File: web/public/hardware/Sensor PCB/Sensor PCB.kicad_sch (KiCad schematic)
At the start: 20 parts, among them J1 Conn_01x08_Pin, J2 Conn_01x08_Pin, J3 Conn_01x06_Pin, J4 Conn_01x06_Pin, U1 DRV5033AJxDBZ, U2 DRV5033AJxDBZ, U3 DRV5033AJxDBZ, U4 DRV5033AJxDBZ, U5 74LS11, U6 74LS11

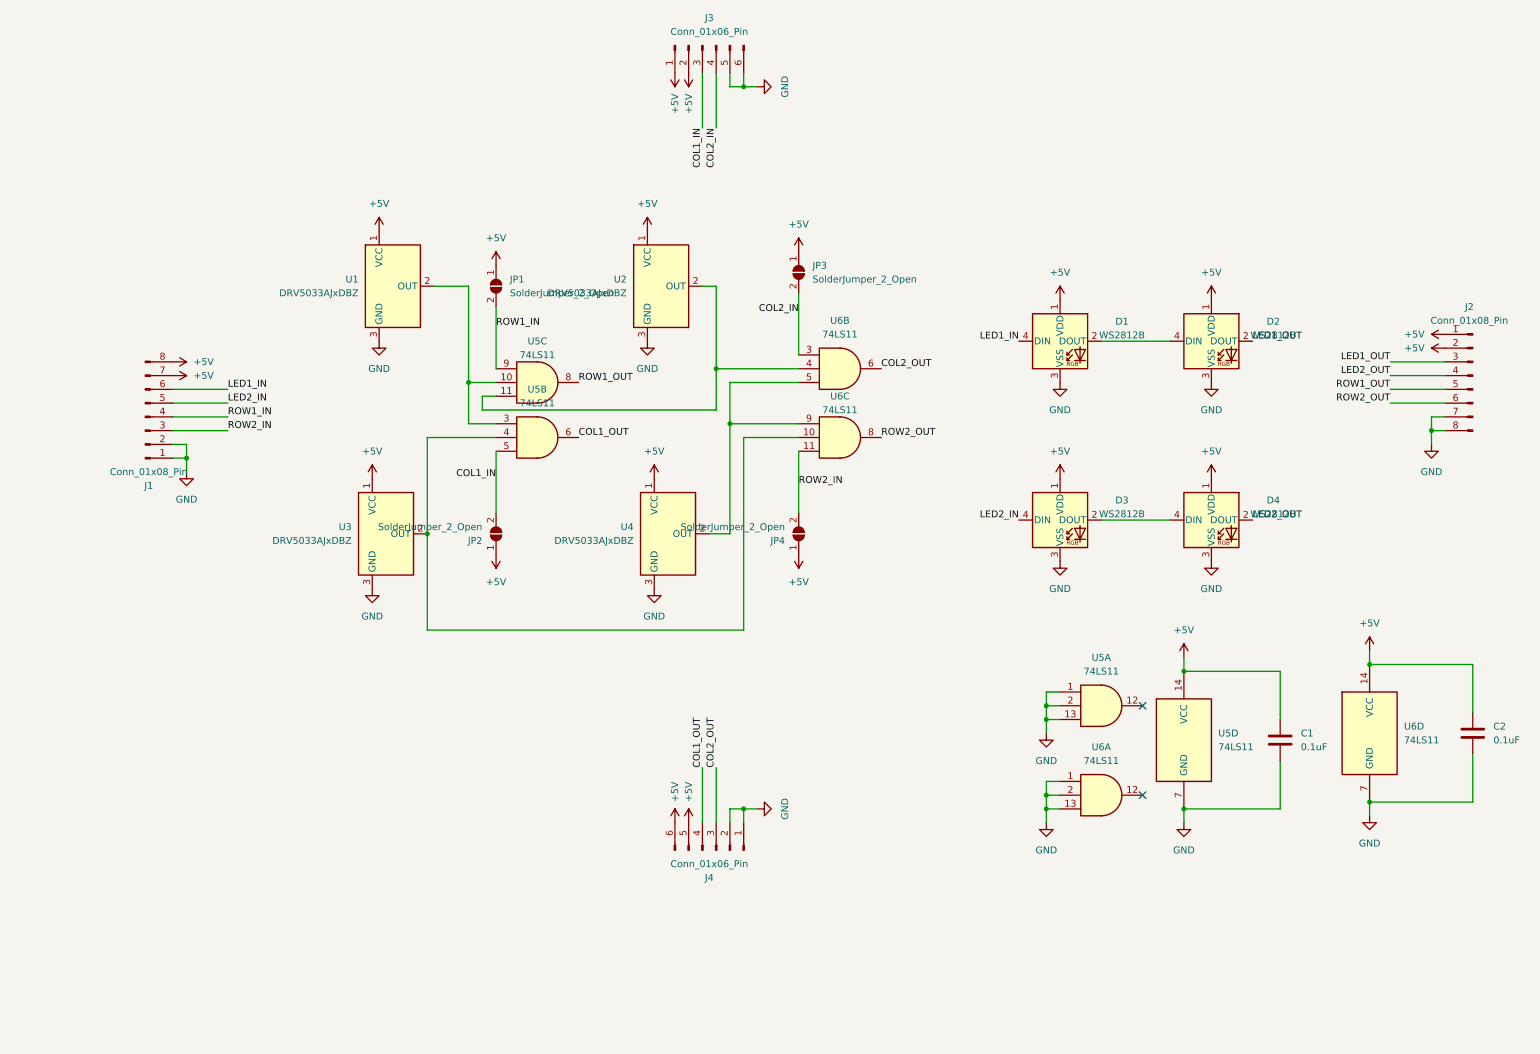
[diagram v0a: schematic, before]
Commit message: Route PCB power and change sch/PCB page size to US letter
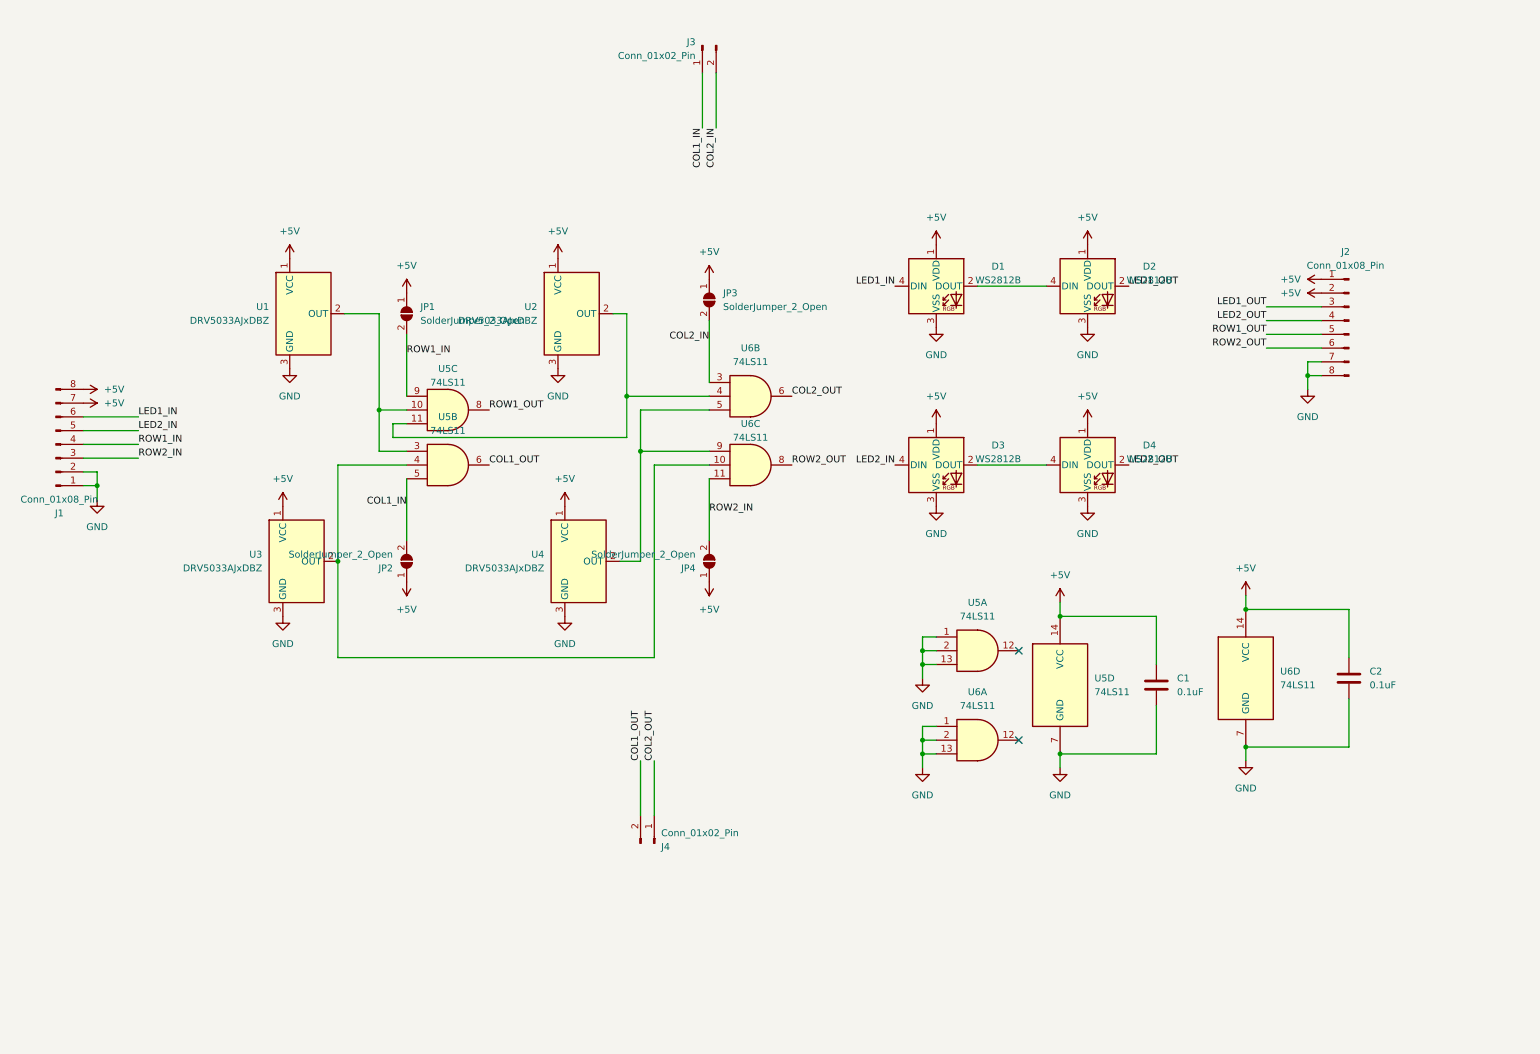
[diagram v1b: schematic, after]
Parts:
- removed J3, J4: Conn_01x06_Pin, Connector_PinHeader_2.54mm:PinHeader_1x06_P2.54mm_Horizontal, symbol Connector:Conn_01x06_Pin
- added J3, J4: Conn_01x02_Pin, Connector_PinHeader_2.54mm:PinHeader_1x02_P2.54mm_Horizontal, symbol Connector:Conn_01x02_Pin
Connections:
- net COL1_IN: now also J3.1 (Pin_1)
- net COL1_OUT: now also J4.2 (Pin_2)
- net COL2_IN: now also J3.2 (Pin_2)
- net COL2_OUT: now also J4.1 (Pin_1)
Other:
- company: (none) -> ECE 477
- title: (none) -> Sensor PCB
- moved on the sheet: C1, C2, D1, D2, D3, D4, J1, J2, JP1, JP2, JP3, JP4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

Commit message: Update production files
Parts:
- added H1, H2, H3: MountingHole, MountingHole:MountingHole_2.7mm_M2.5, symbol Mechanical:MountingHole
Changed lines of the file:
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@@
+    )
+  )
+  (symbol (lib_id "Mechanical:MountingHole") (at 38.1 185.42 0) (unit 1)
+    (in_bom yes) (on_board yes) (dnp no) (fields_autoplaced)
+    (property "Reference" "H3" (at 40.64 184.15 0)
+      (effects (font (size 1.27 1.27)) (justify left))
+    )
+    (property "Value" "MountingHole" (at 40.64 186.69 0)
+      (effects (font (size 1.27 1.27)) (justify left))
+    )
+    (property "Footprint" "MountingHole:MountingHole_2.7mm_M2.5" (at 38.1 185.42 0)
+      (effects (font (size 1.27 1.27)) hide)
+    )
+    (property "Datasheet" "~" (at 38.1 185.42 0)
+      (effects (font (size 1.27 1.27)) hide)
+    )
+    (instances
+      (project "Sensor PCB"
+        (path "/a9f063f9-73a8-44d6-aee6-f41a657d12c2"
+          (reference "H3") (unit 1)
+        )
+      )
     )
   )
@@
     )
   )
+  (symbol (lib_id "Mechanical:MountingHole") (at 38.1 179.07 0) (unit 1)
+    (in_bom yes) (on_board yes) (dnp no) (fields_autoplaced)
+    (property "Reference" "H2" (at 40.64 177.8 0)
+      (effects (font (size 1.27 1.27)) (justify left))
+    )
+    (property "Value" "MountingHole" (at 40.64 180.34 0)
+      (effects (font (size 1.27 1.27)) (justify left))
+    )
+    (property "Footprint" "MountingHole:MountingHole_2.7mm_M2.5" (at 38.1 179.07 0)
+      (effects (font (size 1.27 1.27)) hide)
+    )
+    (property "Datasheet" "~" (at 38.1 179.07 0)
+      (effects (font (size 1.27 1.27)) hide)
+    )
+    (instances
+      (project "Sensor PCB"
+        (path "/a9f063f9-73a8-44d6-aee6-f41a657d12c2"
+          (reference "H2") (unit 1)
+        )
+      )
+    )
+  )
   (symbol (lib_id "power:GND") (at 59.69 121.92 0) (unit 1)
     (in_bom yes) (on_board yes) (dnp no) (fields_autoplaced)
@@
         )
       )
+    )
+  )
+  (symbol (lib_id "Mechanical:MountingHole") (at 38.1 172.72 0) (unit 1)
+    (in_bom yes) (on_board yes) (dnp no) (fields_autoplaced)
+    (property "Reference" "H1" (at 40.64 171.45 0)
+      (effects (font (size 1.27 1.27)) (justify left))
+    )
+    (property "Value" "MountingHole" (at 40.64 173.99 0)
+      (effects (font (size 1.27 1.27)) (justify left))
+    )
+    (property "Footprint" "MountingHole:MountingHole_2.7mm_M2.5" (at 38.1 172.72 0)
+      (effects (font (size 1.27 1.27)) hide)
+    )
+    (property "Datasheet" "~" (at 38.1 172.72 0)
+      (effects (font (size 1.27 1.27)) hide)
+    )
+    (instances
+      (project "Sensor PCB"
+        (path "/a9f063f9-73a8-44d6-aee6-f41a657d12c2"
+          (reference "H1") (unit 1)
+        )
+      )

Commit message: Add pullup resistor to hall effect sensor for open-drain sensors
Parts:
- added R1, R2, R3, R4: 10K, Resistor_SMD:R_0805_2012Metric_Pad1.20x1.40mm_HandSolder, symbol Device:R_Small_US
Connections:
- net +5V: now also R1.1, R2.1, R3.1, R4.1
- net at U2.2 (OUT), U5.11, U6.4: now also R2.2
- net at U4.2 (OUT), U6.5, U6.9: now also R4.2
- net at U1.2 (OUT), U5.10, U5.3: now also R1.2
- net at U3.2 (OUT), U5.4, U6.10: now also R3.2
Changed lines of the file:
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@@
   (junction (at 177.8 144.78) (diameter 0) (color 0 0 0 0)
   )
+  (junction (at 123.19 111.76) (diameter 0) (color 0 0 0 0)
+  )
   (junction (at 237.49 146.05) (diameter 0) (color 0 0 0 0)
   )
@@
   (junction (at 77.47 83.82) (diameter 0) (color 0 0 0 0)
   )
+  (junction (at 69.85 93.98) (diameter 0) (color 0 0 0 0)
+  )
   (junction (at 25.4 97.79) (diameter 0) (color 0 0 0 0)
   )
+  (junction (at 123.19 66.04) (diameter 0) (color 0 0 0 0)
+  )
   (junction (at 203.2 147.32) (diameter 0) (color 0 0 0 0)
   )
   (junction (at 177.8 130.81) (diameter 0) (color 0 0 0 0)
+  )
+  (junction (at 73.66 66.04) (diameter 0) (color 0 0 0 0)
   )
   (junction (at 248.92 77.47) (diameter 0) (color 0 0 0 0)
@@
     (stroke (width 0) (type default))
   )
-  (wire (pts (xy 121.92 111.76) (xy 125.73 111.76))
+  (wire (pts (xy 123.19 55.88) (xy 123.19 58.42))
+    (stroke (width 0) (type default))
+  )
+  (wire (pts (xy 121.92 111.76) (xy 123.19 111.76))
     (stroke (width 0) (type default))
   )
@@
     (stroke (width 0) (type default))
   )
+  (wire (pts (xy 69.85 91.44) (xy 69.85 93.98))
+    (stroke (width 0) (type default))
+  )
   (wire (pts (xy 80.01 88.9) (xy 123.19 88.9))
     (stroke (width 0) (type default))
   )
+  (wire (pts (xy 123.19 109.22) (xy 123.19 111.76))
+    (stroke (width 0) (type default))
+  )
   (wire (pts (xy 177.8 147.32) (xy 180.34 147.32))
     (stroke (width 0) (type default))
@@
     (stroke (width 0) (type default))
   )
-  (wire (pts (xy 71.12 66.04) (xy 77.47 66.04))
+  (wire (pts (xy 73.66 63.5) (xy 73.66 66.04))
+    (stroke (width 0) (type default))
+  )
+  (wire (pts (xy 71.12 66.04) (xy 73.66 66.04))
     (stroke (width 0) (type default))
   )
@@
     (stroke (width 0) (type default))
   )
+  (wire (pts (xy 123.19 111.76) (xy 125.73 111.76))
+    (stroke (width 0) (type default))
+  )
   (wire (pts (xy 251.46 77.47) (xy 248.92 77.47))
     (stroke (width 0) (type default))
@@
     (stroke (width 0) (type default))
   )
+  (wire (pts (xy 123.19 101.6) (xy 123.19 104.14))
+    (stroke (width 0) (type default))
+  )
   (wire (pts (xy 125.73 91.44) (xy 138.43 91.44))
     (stroke (width 0) (type default))
@@
     (stroke (width 0) (type default))
   )
+  (wire (pts (xy 73.66 66.04) (xy 77.47 66.04))
+    (stroke (width 0) (type default))
+  )
+  (wire (pts (xy 69.85 83.82) (xy 69.85 86.36))
+    (stroke (width 0) (type default))
+  )
   (wire (pts (xy 25.4 95.25) (xy 25.4 97.79))
     (stroke (width 0) (type default))
@@
   )
   (wire (pts (xy 248.92 77.47) (xy 248.92 80.01))
+    (stroke (width 0) (type default))
+  )
+  (wire (pts (xy 123.19 63.5) (xy 123.19 66.04))
+    (stroke (width 0) (type default))
+  )
+  (wire (pts (xy 73.66 55.88) (xy 73.66 58.42))
     (stroke (width 0) (type default))
   )
@@
   (label "COL2_OUT" (at 153.67 81.28 0) (fields_autoplaced)
     (effects (font (size 1.27 1.27)) (justify left bottom))
+  )
+  (symbol (lib_id "power:+5V") (at 73.66 55.88 0) (unit 1)
+    (in_bom yes) (on_board yes) (dnp no)
+    (property "Reference" "#PWR025" (at 73.66 59.69 0)
+      (effects (font (size 1.27 1.27)) hide)
+    )
+    (property "Value" "+5V" (at 73.66 52.07 0)
+      (effects (font (size 1.27 1.27)))
+    )
+    (property "Footprint" "" (at 73.66 55.88 0)
+      (effects (font (size 1.27 1.27)) hide)
+    )
+    (property "Datasheet" "" (at 73.66 55.88 0)
+      (effects (font (size 1.27 1.27)) hide)
+    )
+    (pin "1")
+    (instances
+      (project "Sensor PCB"
+        (path "/a9f063f9-73a8-44d6-aee6-f41a657d12c2"
+          (reference "#PWR025") (unit 1)
+        )
+      )
+    )
   )
   (symbol (lib_id "power:+5V") (at 251.46 62.23 90) (mirror x) (unit 1)
@@
     )
   )
+  (symbol (lib_id "Device:R_Small_US") (at 123.19 106.68 0) (unit 1)
+    (in_bom yes) (on_board yes) (dnp no) (fields_autoplaced)
+    (property "Reference" "R4" (at 125.73 105.41 0)
+      (effects (font (size 1.27 1.27)) (justify left))
+    )
+    (property "Value" "10K" (at 125.73 107.95 0)
+      (effects (font (size 1.27 1.27)) (justify left))
+    )
+    (property "Footprint" "Resistor_SMD:R_0805_2012Metric_Pad1.20x1.40mm_HandSolder" (at 123.19 106.68 0)
+      (effects (font (size 1.27 1.27)) hide)
+    )
+    (property "Datasheet" "~" (at 123.19 106.68 0)
+      (effects (font (size 1.27 1.27)) hide)
+    )
+    (pin "1")
+    (pin "2")
+    (instances
+      (project "Sensor PCB"
+        (path "/a9f063f9-73a8-44d6-aee6-f41a657d12c2"
+          (reference "R4") (unit 1)
+        )
+      )
+    )
+  )
   (symbol (lib_id "power:GND") (at 180.34 68.58 0) (mirror y) (unit 1)
     (in_bom yes) (on_board yes) (dnp no) (fields_autoplaced)
@@
         (path "/a9f063f9-73a8-44d6-aee6-f41a657d12c2"
           (reference "#PWR021") (unit 1)
+        )
+      )
+    )
+  )
+  (symbol (lib_id "power:+5V") (at 123.19 101.6 0) (unit 1)
+    (in_bom yes) (on_board yes) (dnp no)
+    (property "Reference" "#PWR028" (at 123.19 105.41 0)
+      (effects (font (size 1.27 1.27)) hide)
+    )
+    (property "Value" "+5V" (at 123.19 97.79 0)
+      (effects (font (size 1.27 1.27)))
+    )
+    (property "Footprint" "" (at 123.19 101.6 0)
+      (effects (font (size 1.27 1.27)) hide)
+    )
+    (property "Datasheet" "" (at 123.19 101.6 0)
+      (effects (font (size 1.27 1.27)) hide)
+    )
+    (pin "1")
+    (instances
+      (project "Sensor PCB"
+        (path "/a9f063f9-73a8-44d6-aee6-f41a657d12c2"
+          (reference "#PWR028") (unit 1)
         )
       )
@@
     )
   )
+  (symbol (lib_id "Device:R_Small_US") (at 73.66 60.96 0) (unit 1)
+    (in_bom yes) (on_board yes) (dnp no) (fields_autoplaced)
+    (property "Reference" "R1" (at 76.2 59.69 0)
+      (effects (font (size 1.27 1.27)) (justify left))
+    )
+    (property "Value" "10K" (at 76.2 62.23 0)
+      (effects (font (size 1.27 1.27)) (justify left))
+    )
+    (property "Footprint" "Resistor_SMD:R_0805_2012Metric_Pad1.20x1.40mm_HandSolder" (at 73.66 60.96 0)
+      (effects (font (size 1.27 1.27)) hide)
+    )
+    (property "Datasheet" "~" (at 73.66 60.96 0)
+      (effects (font (size 1.27 1.27)) hide)
+    )
+    (pin "1")
+    (pin "2")
+    (instances
+      (project "Sensor PCB"
+        (path "/a9f063f9-73a8-44d6-aee6-f41a657d12c2"
+          (reference "R1") (unit 1)
+        )
+      )
+    )
+  )
   (symbol (lib_id "Connector:Conn_01x02_Pin") (at 128.27 163.83 270) (mirror x) (unit 1)
     (in_bom yes) (on_board yes) (dnp no)
@@
     )
   )
+  (symbol (lib_id "Device:R_Small_US") (at 123.19 60.96 0) (unit 1)
+    (in_bom yes) (on_board yes) (dnp no) (fields_autoplaced)
+    (property "Reference" "R2" (at 125.73 59.69 0)
+      (effects (font (size 1.27 1.27)) (justify left))
+    )
+    (property "Value" "10K" (at 125.73 62.23 0)
+      (effects (font (size 1.27 1.27)) (justify left))
+    )
+    (property "Footprint" "Resistor_SMD:R_0805_2012Metric_Pad1.20x1.40mm_HandSolder" (at 123.19 60.96 0)
+      (effects (font (size 1.27 1.27)) hide)
+    )
+    (property "Datasheet" "~" (at 123.19 60.96 0)
+      (effects (font (size 1.27 1.27)) hide)
+    )
+    (pin "1")
+    (pin "2")
+    (instances
+      (project "Sensor PCB"
+        (path "/a9f063f9-73a8-44d6-aee6-f41a657d12c2"
+          (reference "R2") (unit 1)
+        )
+      )
+    )
+  )
   (symbol (lib_id "Sensor_Magnetic:DRV5033AJxDBZ") (at 62.23 111.76 0) (unit 1)
     (in_bom yes) (on_board yes) (dnp no) (fields_autoplaced)
@@
         (path "/a9f063f9-73a8-44d6-aee6-f41a657d12c2"
           (reference "D4") (unit 1)
+        )
+      )
+    )
+  )
+  (symbol (lib_id "Device:R_Small_US") (at 69.85 88.9 0) (unit 1)
+    (in_bom yes) (on_board yes) (dnp no) (fields_autoplaced)
+    (property "Reference" "R3" (at 72.39 87.63 0)
+      (effects (font (size 1.27 1.27)) (justify left))
+    )
+    (property "Value" "10K" (at 72.39 90.17 0)
+      (effects (font (size 1.27 1.27)) (justify left))
+    )
+    (property "Footprint" "Resistor_SMD:R_0805_2012Metric_Pad1.20x1.40mm_HandSolder" (at 69.85 88.9 0)
+      (effects (font (size 1.27 1.27)) hide)
+    )
+    (property "Datasheet" "~" (at 69.85 88.9 0)
+      (effects (font (size 1.27 1.27)) hide)
+    )
+    (pin "1")
+    (pin "2")
+    (instances
+      (project "Sensor PCB"
+        (path "/a9f063f9-73a8-44d6-aee6-f41a657d12c2"
+          (reference "R3") (unit 1)
         )
       )
@@
     )
   )
+  (symbol (lib_id "power:+5V") (at 69.85 83.82 0) (unit 1)
+    (in_bom yes) (on_board yes) (dnp no)
+    (property "Reference" "#PWR026" (at 69.85 87.63 0)
+      (effects (font (size 1.27 1.27)) hide)
+    )
+    (property "Value" "+5V" (at 69.85 80.01 0)
+      (effects (font (size 1.27 1.27)))
+    )
+    (property "Footprint" "" (at 69.85 83.82 0)
+      (effects (font (size 1.27 1.27)) hide)
+    )
+    (property "Datasheet" "" (at 69.85 83.82 0)
+      (effects (font (size 1.27 1.27)) hide)
+    )
+    (pin "1")
+    (instances
+      (project "Sensor PCB"
+        (path "/a9f063f9-73a8-44d6-aee6-f41a657d12c2"
+          (reference "#PWR026") (unit 1)
+        )
+      )
+    )
+  )
   (symbol (lib_id "LED:WS2812B") (at 180.34 93.98 0) (unit 1)
     (in_bom yes) (on_board yes) (dnp no) (fields_autoplaced)
@@
         )
       )
+    )
+  )
+  (symbol (lib_id "power:+5V") (at 123.19 55.88 0) (unit 1)
+    (in_bom yes) (on_board yes) (dnp no)
+    (property "Reference" "#PWR027" (at 123.19 59.69 0)
+      (effects (font (size 1.27 1.27)) hide)
+    )
+    (property "Value" "+5V" (at 123.19 52.07 0)
+      (effects (font (size 1.27 1.27)))
+    )
+    (property "Footprint" "" (at 123.19 55.88 0)
+      (effects (font (size 1.27 1.27)) hide)
+    )
+    (property "Datasheet" "" (at 123.19 55.88 0)
+      (effects (font (size 1.27 1.27)) hide)
+    )
+    (pin "1")
+    (instances
+      (project "Sensor PCB"
+        (path "/a9f063f9-73a8-44d6-aee6-f41a657d12c2"
+          (reference "#PWR027") (unit 1)
+        )
+      )
